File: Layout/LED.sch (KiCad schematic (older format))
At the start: 6 parts

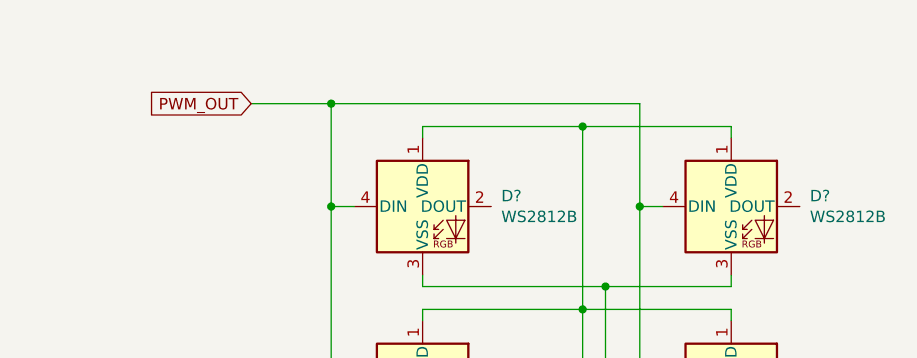
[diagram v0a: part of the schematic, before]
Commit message: Add voltage regulators
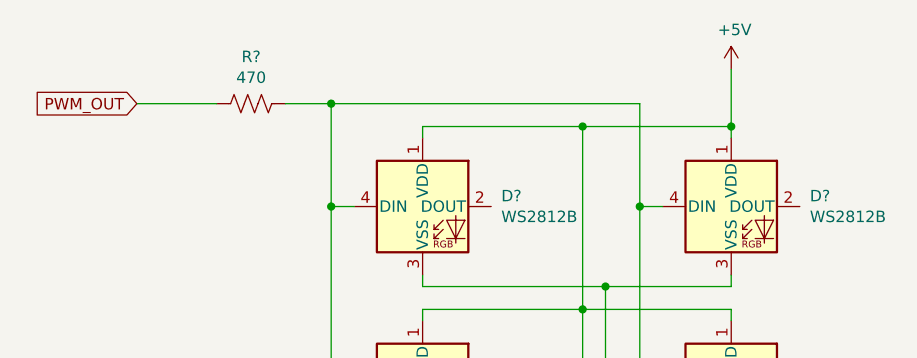
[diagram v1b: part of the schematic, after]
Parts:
- added R?: 470, symbol Device:R_US
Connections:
- net PWM_OUT: now also R?.2; no longer D?.4 (DIN), D?.4 (DIN), D?.4 (DIN), D?.4 (DIN), D?.4 (DIN), D?.4 (DIN)
- net +5V: now reaches D?.1 (VDD), D?.1 (VDD), D?.1 (VDD), D?.1 (VDD), D?.1 (VDD), D?.1 (VDD)
- new net: D?.4 (DIN), D?.4 (DIN), D?.4 (DIN), D?.4 (DIN), D?.4 (DIN), D?.4 (DIN), R?.1
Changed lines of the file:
@@
 $EndComp
 Connection ~ 6300 4950
-Text GLabel 4200 2550 0    50   Input ~ 0
+Text GLabel 3700 2550 0    50   Input ~ 0
 PWM_OUT
+$Comp
+L Device:R_US R?
+U 1 1 5F35CE0C
+P 4200 2550
+F 0 "R?" V 3995 2550 50  0000 C CNN
+F 1 "470" V 4086 2550 50  0000 C CNN
+F 2 "" V 4240 2540 50  0001 C CNN
+F 3 "~" H 4200 2550 50  0001 C CNN
+	1    4200 2550
+	0    1    1    0
+$EndComp
+Connection ~ 4550 2550
 Wire Wire Line
-	4200 2550 4550 2550
-Connection ~ 4550 2550
+	4350 2550 4550 2550
+Wire Wire Line
+	4050 2550 3700 2550
+$Comp
+L power:+5V #PWR?
+U 1 1 5F35EAE9
+P 6300 2400
+F 0 "#PWR?" H 6300 2250 50  0001 C CNN
+F 1 "+5V" H 6315 2573 50  0000 C CNN
+F 2 "" H 6300 2400 50  0001 C CNN
+F 3 "" H 6300 2400 50  0001 C CNN
+	1    6300 2400
+	1    0    0    -1
+$EndComp
+Wire Wire Line
+	6300 2400 6300 2650
+Connection ~ 6300 2650
 $EndSCHEMATC

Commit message: Add footprints
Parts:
- R?: footprint (none) -> Resistor_SMD:R_0603_1608Metric_Pad1.05x0.95mm_HandSolder
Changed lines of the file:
@@
 F 0 "R?" V 3995 2550 50  0000 C CNN
 F 1 "470" V 4086 2550 50  0000 C CNN
-F 2 "" V 4240 2540 50  0001 C CNN
+F 2 "Resistor_SMD:R_0603_1608Metric_Pad1.05x0.95mm_HandSolder" V 4240 2540 50  0001 C CNN
 F 3 "~" H 4200 2550 50  0001 C CNN
 	1    4200 2550

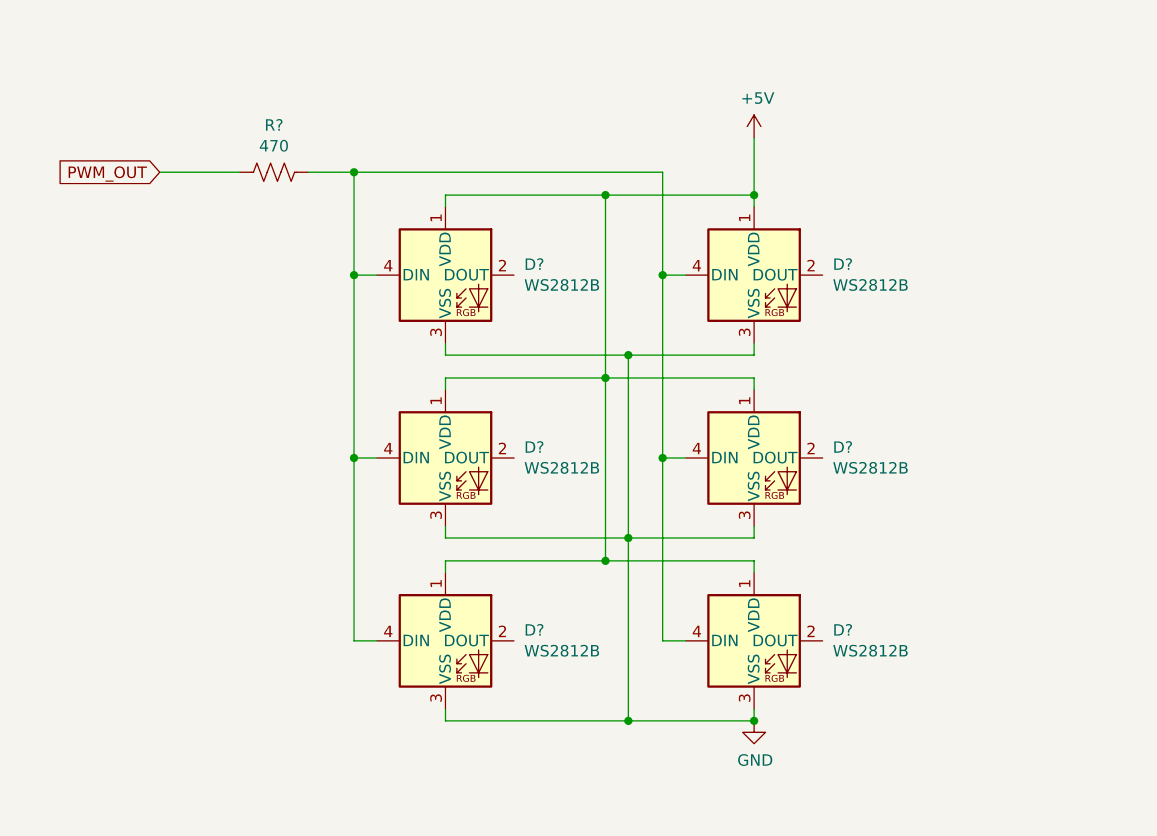
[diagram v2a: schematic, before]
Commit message: Add logic translator for LED
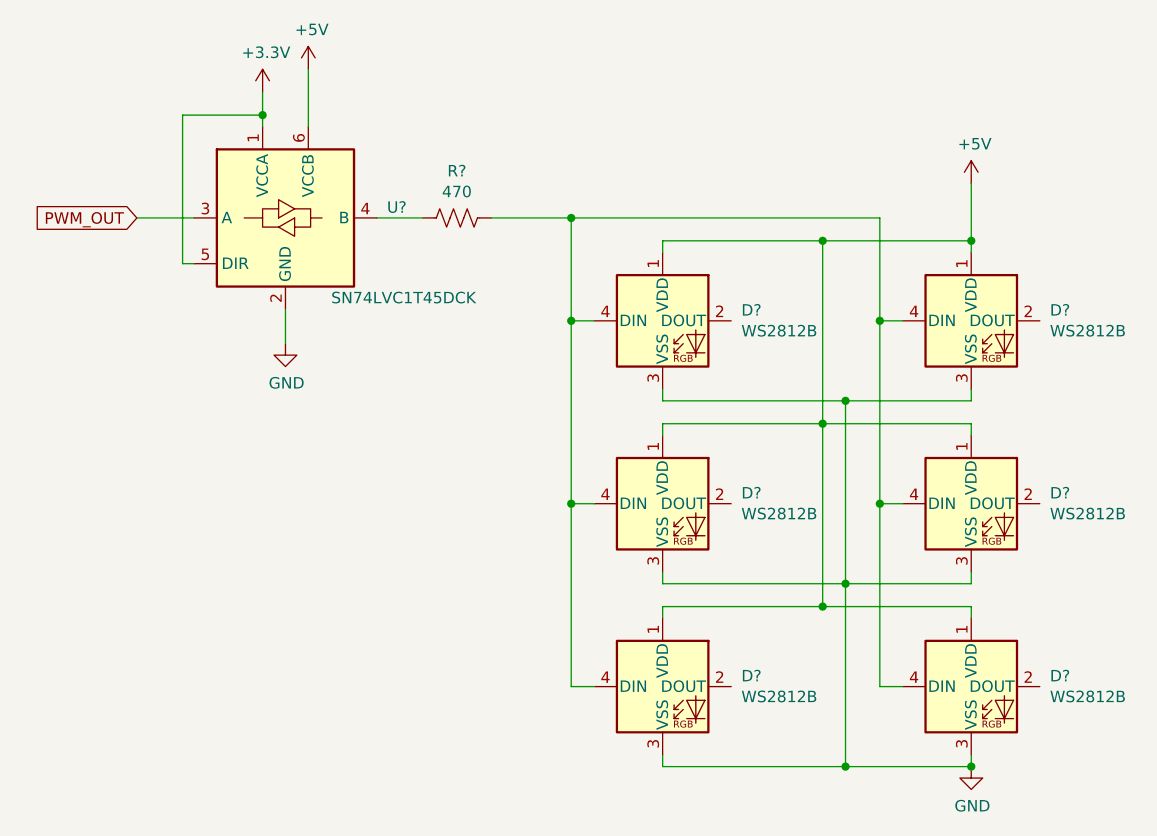
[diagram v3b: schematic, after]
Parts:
- added U?: SN74LVC1T45DCK, Package_TO_SOT_SMD:SOT-363_SC-70-6, symbol Logic_LevelTranslator:SN74LVC1T45DCK
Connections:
- net +5V: now also U?.6 (VCCB)
- net GND: now also U?.2 (GND)
- net PWM_OUT: now also U?.3 (A); no longer R?.2
- new net: R?.2, U?.4 (B)
- new net +3V3: U?.1 (VCCA), U?.5 (DIR)
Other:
- moved on the sheet: D?, R?

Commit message: Update footprints and references
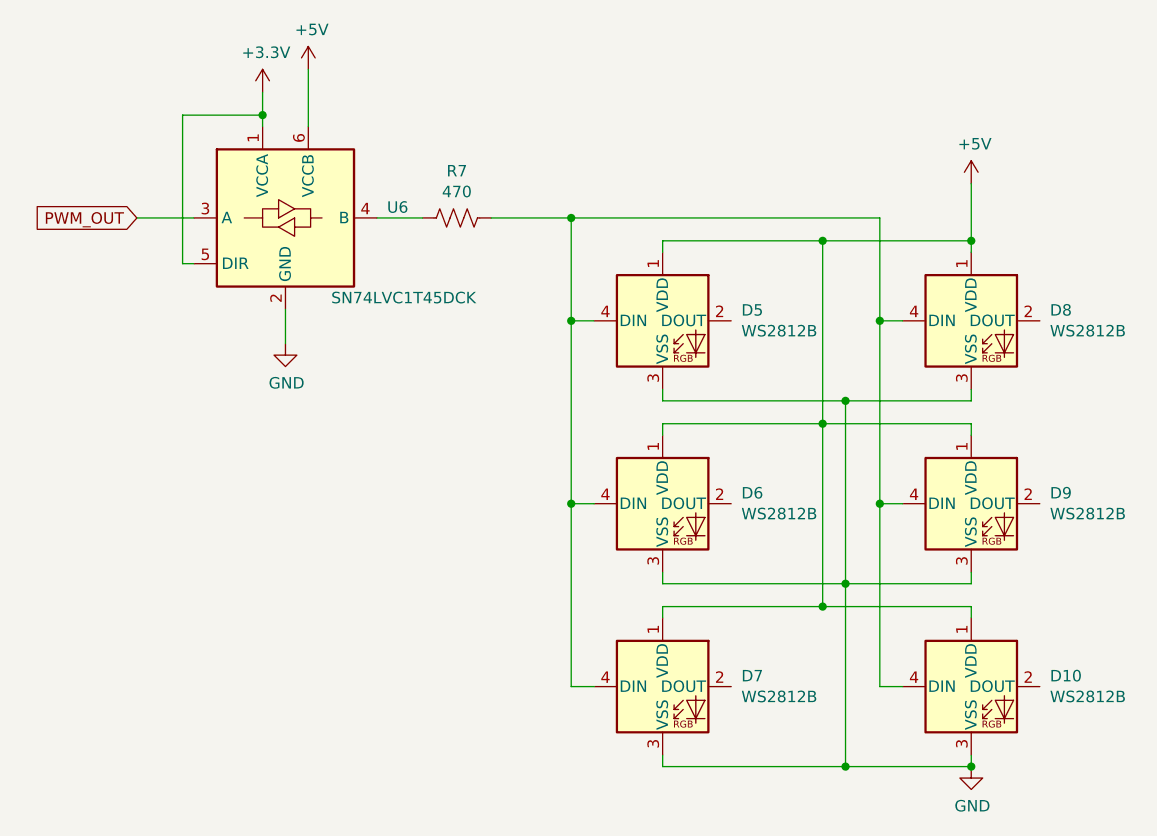
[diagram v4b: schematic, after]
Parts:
- gave numbers to parts that had none: 8
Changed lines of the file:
@@
 $EndDescr
 $Comp
-L LED:WS2812B D?
+L LED:WS2812B D5
 U 1 1 5F39761B
 P 5900 3200
-F 0 "D?" H 6244 3246 50  0000 L CNN
+F 0 "D5" H 6244 3246 50  0000 L CNN
 F 1 "WS2812B" H 6244 3155 50  0000 L CNN
 F 2 "LED_SMD:LED_WS2812B_PLCC4_5.0x5.0mm_P3.2mm" H 5950 2900 50  0001 L TNN
@@
 $EndComp
 $Comp
-L LED:WS2812B D?
+L LED:WS2812B D6
 U 1 1 5F397A9B
 P 5900 4000
-F 0 "D?" H 6244 4046 50  0000 L CNN
+F 0 "D6" H 6244 4046 50  0000 L CNN
 F 1 "WS2812B" H 6244 3955 50  0000 L CNN
 F 2 "LED_SMD:LED_WS2812B_PLCC4_5.0x5.0mm_P3.2mm" H 5950 3700 50  0001 L TNN
@@
 $EndComp
 $Comp
-L LED:WS2812B D?
+L LED:WS2812B D7
 U 1 1 5F3982E1
 P 5900 4800
-F 0 "D?" H 6244 4846 50  0000 L CNN
+F 0 "D7" H 6244 4846 50  0000 L CNN
 F 1 "WS2812B" H 6244 4755 50  0000 L CNN
 F 2 "LED_SMD:LED_WS2812B_PLCC4_5.0x5.0mm_P3.2mm" H 5950 4500 50  0001 L TNN
@@
 $EndComp
 $Comp
-L LED:WS2812B D?
+L LED:WS2812B D8
 U 1 1 5F3986FD
 P 7250 3200
-F 0 "D?" H 7594 3246 50  0000 L CNN
+F 0 "D8" H 7594 3246 50  0000 L CNN
 F 1 "WS2812B" H 7594 3155 50  0000 L CNN
 F 2 "LED_SMD:LED_WS2812B_PLCC4_5.0x5.0mm_P3.2mm" H 7300 2900 50  0001 L TNN
@@
 $EndComp
 $Comp
-L LED:WS2812B D?
+L LED:WS2812B D9
 U 1 1 5F398CFA
 P 7250 4000
-F 0 "D?" H 7594 4046 50  0000 L CNN
+F 0 "D9" H 7594 4046 50  0000 L CNN
 F 1 "WS2812B" H 7594 3955 50  0000 L CNN
 F 2 "LED_SMD:LED_WS2812B_PLCC4_5.0x5.0mm_P3.2mm" H 7300 3700 50  0001 L TNN
@@
 $EndComp
 $Comp
-L LED:WS2812B D?
+L LED:WS2812B D10
 U 1 1 5F399728
 P 7250 4800
-F 0 "D?" H 7594 4846 50  0000 L CNN
+F 0 "D10" H 7594 4846 50  0000 L CNN
 F 1 "WS2812B" H 7594 4755 50  0000 L CNN
 F 2 "LED_SMD:LED_WS2812B_PLCC4_5.0x5.0mm_P3.2mm" H 7300 4500 50  0001 L TNN
@@
 Connection ~ 6850 3200
 $Comp
-L power:GND #PWR?
+L power:GND #PWR0135
 U 1 1 5F3A2924
 P 7250 5150
-F 0 "#PWR?" H 7250 4900 50  0001 C CNN
+F 0 "#PWR0135" H 7250 4900 50  0001 C CNN
 F 1 "GND" H 7255 4977 50  0000 C CNN
 F 2 "" H 7250 5150 50  0001 C CNN
@@
 PWM_OUT
 $Comp
-L Device:R_US R?
+L Device:R_US R7
 U 1 1 5F35CE0C
 P 5000 2750
-F 0 "R?" V 4795 2750 50  0000 C CNN
+F 0 "R7" V 4795 2750 50  0000 C CNN
 F 1 "470" V 4886 2750 50  0000 C CNN
 F 2 "Resistor_SMD:R_0603_1608Metric_Pad1.05x0.95mm_HandSolder" V 5040 2740 50  0001 C CNN
@@
 Connection ~ 5500 2750
 $Comp
-L power:+5V #PWR?
+L power:+5V #PWR0136
 U 1 1 5F35EAE9
 P 7250 2600
-F 0 "#PWR?" H 7250 2450 50  0001 C CNN
+F 0 "#PWR0136" H 7250 2450 50  0001 C CNN
 F 1 "+5V" H 7265 2773 50  0000 C CNN
 F 2 "" H 7250 2600 50  0001 C CNN
@@
 	3600 2750 3850 2750
 $Comp
-L power:GND #PWR?
+L power:GND #PWR0137
 U 1 1 5F3A5F3B
 P 4250 3300
-F 0 "#PWR?" H 4250 3050 50  0001 C CNN
+F 0 "#PWR0137" H 4250 3050 50  0001 C CNN
 F 1 "GND" H 4255 3127 50  0000 C CNN
 F 2 "" H 4250 3300 50  0001 C CNN
@@
 $EndComp
 $Comp
-L power:+3.3V #PWR?
+L power:+3.3V #PWR0138
 U 1 1 5F3A72E1
 P 4150 2200
-F 0 "#PWR?" H 4150 2050 50  0001 C CNN
+F 0 "#PWR0138" H 4150 2050 50  0001 C CNN
 F 1 "+3.3V" H 4165 2373 50  0000 C CNN
 F 2 "" H 4150 2200 50  0001 C CNN
@@
 $EndComp
 $Comp
-L power:+5V #PWR?
+L power:+5V #PWR0139
 U 1 1 5F3A77B2
 P 4350 2100
-F 0 "#PWR?" H 4350 1950 50  0001 C CNN
+F 0 "#PWR0139" H 4350 1950 50  0001 C CNN
 F 1 "+5V" H 4365 2273 50  0000 C CNN
 F 2 "" H 4350 2100 50  0001 C CNN
@@
 $EndComp
 $Comp
-L Logic_LevelTranslator:SN74LVC1T45DCK U?
+L Logic_LevelTranslator:SN74LVC1T45DCK U6
 U 1 1 5F3A9942
 P 4250 2750
-F 0 "U?" H 4694 2796 50  0000 L CNN
+F 0 "U6" H 4694 2796 50  0000 L CNN
 F 1 "SN74LVC1T45DCK" H 4450 2400 50  0000 L CNN
 F 2 "Package_TO_SOT_SMD:SOT-363_SC-70-6" H 4250 2300 50  0001 C CNN
